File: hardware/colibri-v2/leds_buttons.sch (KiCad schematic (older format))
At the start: 36 parts, among them SW1 SW_PUSH, SW2 SW_PUSH, SW3 SW_PUSH, SW4 SW_PUSH, SW5 SW_PUSH, SW6 SW_PUSH, SW7 SW_PUSH

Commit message: Changes to BOOT0
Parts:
- removed C32: 100nF, symbol C
- added R?: 10K, symbol R
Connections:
- net BOOT0: now also R?.2
- net GND: now also R?.1; no longer SW5.2
- net VDD: now also SW5.2
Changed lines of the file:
@@
 	1    0    0    -1
 $EndComp
-Wire Wire Line
-	1600 3850 1600 3650
-Wire Wire Line
-	2050 2950 2500 2950
-Connection ~ 2350 2950
-Wire Wire Line
-	1350 2950 1750 2950
 $Comp
 L SW_PUSH SW3
@@
 	-1   0    0    1
 $EndComp
-Wire Wire Line
-	3100 4750 3250 4750
-Wire Wire Line
-	3250 4400 3250 4900
 $Comp
 L C C30
@@
 	1    0    0    -1
 $EndComp
-Wire Wire Line
-	3250 5650 3250 5600
-Connection ~ 3250 4750
-Wire Wire Line
-	2350 5650 2350 5400
-Wire Wire Line
-	2050 4750 2500 4750
-Wire Wire Line
-	2350 5100 2350 4750
-Connection ~ 2350 4750
-Wire Wire Line
-	1750 4750 1350 4750
 $Comp
 L R R27
@@
 	-1   0    0    1
 $EndComp
-Wire Wire Line
-	3250 5300 3250 5200
 $Comp
 L SW_PUSH SW4
@@
 	-1   0    0    1
 $EndComp
-Wire Wire Line
-	3100 6600 3250 6600
-Wire Wire Line
-	3250 6250 3250 6750
 $Comp
 L C C31
@@
 	1    0    0    -1
 $EndComp
-Wire Wire Line
-	3250 7500 3250 7450
-Connection ~ 3250 6600
-Wire Wire Line
-	2350 7500 2350 7250
-Wire Wire Line
-	2050 6600 2500 6600
-Wire Wire Line
-	2350 6950 2350 6600
-Connection ~ 2350 6600
-Wire Wire Line
-	1750 6600 1350 6600
 $Comp
 L R R28
@@
 	-1   0    0    1
 $EndComp
-Wire Wire Line
-	3250 7150 3250 7050
 $Comp
 L SW_PUSH SW6
@@
 	-1   0    0    1
 $EndComp
-Wire Wire Line
-	6050 2950 6200 2950
-Wire Wire Line
-	6200 2600 6200 3100
 $Comp
 L C C33
@@
 	1    0    0    -1
 $EndComp
-Wire Wire Line
-	6200 3850 6200 3800
-Connection ~ 6200 2950
-Wire Wire Line
-	5300 3850 5300 3600
-Wire Wire Line
-	5000 2950 5450 2950
-Wire Wire Line
-	5300 3300 5300 2950
-Connection ~ 5300 2950
-Wire Wire Line
-	4700 2950 4300 2950
 $Comp
 L R R33
@@
 	-1   0    0    1
 $EndComp
-Wire Wire Line
-	6200 3500 6200 3400
 $Comp
 L SW_PUSH SW7
@@
 	-1   0    0    1
 $EndComp
-Wire Wire Line
-	6050 4750 6200 4750
-Wire Wire Line
-	6200 4400 6200 4900
 $Comp
 L C C34
@@
 	1    0    0    -1
 $EndComp
-Wire Wire Line
-	6200 5650 6200 5600
-Connection ~ 6200 4750
-Wire Wire Line
-	5300 5650 5300 5400
-Wire Wire Line
-	5000 4750 5450 4750
-Wire Wire Line
-	5300 5100 5300 4750
-Connection ~ 5300 4750
-Wire Wire Line
-	4700 4750 4300 4750
 $Comp
 L R R34
@@
 	-1   0    0    1
 $EndComp
-Wire Wire Line
-	6200 5300 6200 5200
 $Comp
 L VDD #PWR24
@@
 	1    0    0    -1
 $EndComp
-Wire Wire Line
-	3250 1750 3250 1200
-Wire Wire Line
-	3250 1200 3100 1200
 Text HLabel 1350 1200 0    60   Output ~ 0
 RESET#
@@
 	0    1    1    0
 $EndComp
-Wire Wire Line
-	10100 1200 9650 1200
-Wire Wire Line
-	9650 1500 10100 1500
-Connection ~ 10100 1500
-Wire Wire Line
-	9650 1800 10100 1800
-Connection ~ 10100 1800
-Wire Wire Line
-	10100 2100 9650 2100
-Wire Wire Line
-	8900 1200 9250 1200
-Wire Wire Line
-	8900 1500 9250 1500
-Wire Wire Line
-	8900 1800 9250 1800
-Wire Wire Line
-	8900 2100 9250 2100
 Text HLabel 8200 1200 0    60   Input ~ 0
 LED1
@@
 Text HLabel 8200 2100 0    60   Input ~ 0
 LED4
-Wire Wire Line
-	8200 1200 8600 1200
-Wire Wire Line
-	8200 1500 8600 1500
-Wire Wire Line
-	8200 1800 8600 1800
-Wire Wire Line
-	8200 2100 8600 2100
 $Comp
 L GND #PWR23
@@
 	1    0    0    -1
 $EndComp
-$Comp
-L C C32
-U 1 1 56075502
-P 5300 1450
-F 0 "C32" H 5325 1550 50  0000 L CNN
-F 1 "100nF" H 5325 1350 50  0000 L CNN
-F 2 "" H 5338 1300 30  0000 C CNN
-F 3 "" H 5300 1450 60  0000 C CNN
-	1    5300 1450
-	1    0    0    -1
-$EndComp
-$Comp
-L GND #PWR30
-U 1 1 56075508
-P 5300 1750
-F 0 "#PWR30" H 5300 1500 50  0001 C CNN
-F 1 "GND" H 5300 1600 50  0000 C CNN
-F 2 "" H 5300 1750 60  0000 C CNN
-F 3 "" H 5300 1750 60  0000 C CNN
-	1    5300 1750
-	1    0    0    -1
-$EndComp
-Wire Wire Line
-	5300 1600 5300 1750
-Wire Wire Line
-	6200 1750 6200 1200
-Wire Wire Line
-	6200 1200 6050 1200
-Wire Wire Line
-	5300 1200 5300 1300
-Wire Wire Line
-	4300 1200 5450 1200
-Connection ~ 5300 1200
 Text HLabel 4300 1200 0    60   Output ~ 0
 BOOT0
-$Comp
-L GND #PWR33
-U 1 1 56075518
-P 6200 1750
-F 0 "#PWR33" H 6200 1500 50  0001 C CNN
-F 1 "GND" H 6200 1600 50  0000 C CNN
-F 2 "" H 6200 1750 60  0000 C CNN
-F 3 "" H 6200 1750 60  0000 C CNN
-	1    6200 1750
-	1    0    0    -1
-$EndComp
 $Comp
 L R R?
@@
 	0    1    1    0
 $EndComp
-Wire Wire Line
-	1350 1200 1750 1200
-Wire Wire Line
-	2050 1200 2500 1200
-Wire Wire Line
-	2350 2400 2350 2500
-Wire Wire Line
-	2350 2800 2350 2950
-Wire Wire Line
-	1600 3350 1600 2950
-Connection ~ 1600 2950
 $Comp
 L GND #PWR?
@@
 	1    0    0    -1
 $EndComp
-Wire Wire Line
-	3100 2950 3300 2950
-Wire Wire Line
-	3300 2950 3300 3850
-Wire Wire Line
-	10100 950  10100 2100
 $Comp
 L VDD #PWR?
@@
 	1    0    0    -1
 $EndComp
+$Comp
+L R R?
+U 1 1 5622C644
+P 4900 1550
+F 0 "R?" V 4980 1550 50  0000 C CNN
+F 1 "10K" V 4900 1550 50  0000 C CNN
+F 2 "" V 4830 1550 30  0000 C CNN
+F 3 "" H 4900 1550 30  0000 C CNN
+	1    4900 1550
+	-1   0    0    1
+$EndComp
+$Comp
+L VDD #PWR?
+U 1 1 5622CB72
+P 6200 1000
+F 0 "#PWR?" H 6200 850 50  0001 C CNN
+F 1 "VDD" H 6200 1150 50  0000 C CNN
+F 2 "" H 6200 1000 60  0000 C CNN
+F 3 "" H 6200 1000 60  0000 C CNN
+	1    6200 1000
+	1    0    0    -1
+$EndComp
+$Comp
+L GND #PWR?
+U 1 1 5622D3C9
+P 4900 1900
+F 0 "#PWR?" H 4900 1650 50  0001 C CNN
+F 1 "GND" H 4900 1750 50  0000 C CNN
+F 2 "" H 4900 1900 60  0000 C CNN
+F 3 "" H 4900 1900 60  0000 C CNN
+	1    4900 1900
+	1    0    0    -1
+$EndComp
+Wire Wire Line
+	1600 3850 1600 3650
+Wire Wire Line
+	2050 2950 2500 2950
+Connection ~ 2350 2950
+Wire Wire Line
+	1350 2950 1750 2950
+Wire Wire Line
+	3100 4750 3250 4750
+Wire Wire Line
+	3250 4400 3250 4900
+Wire Wire Line
+	3250 5650 3250 5600
+Connection ~ 3250 4750
+Wire Wire Line
+	2350 5650 2350 5400
+Wire Wire Line
+	2050 4750 2500 4750
+Wire Wire Line
+	2350 5100 2350 4750
+Connection ~ 2350 4750
+Wire Wire Line
+	1750 4750 1350 4750
+Wire Wire Line
+	3250 5300 3250 5200
+Wire Wire Line
+	3100 6600 3250 6600
+Wire Wire Line
+	3250 6250 3250 6750
+Wire Wire Line
+	3250 7500 3250 7450
+Connection ~ 3250 6600
+Wire Wire Line
+	2350 7500 2350 7250
+Wire Wire Line
+	2050 6600 2500 6600
+Wire Wire Line
+	2350 6950 2350 6600
+Connection ~ 2350 6600
+Wire Wire Line
+	1750 6600 1350 6600
+Wire Wire Line
+	3250 7150 3250 7050
+Wire Wire Line
+	6050 2950 6200 2950
+Wire Wire Line
+	6200 2600 6200 3100
+Wire Wire Line
+	6200 3850 6200 3800
+Connection ~ 6200 2950
+Wire Wire Line
+	5300 3850 5300 3600
+Wire Wire Line
+	5000 2950 5450 2950
+Wire Wire Line
+	5300 3300 5300 2950
+Connection ~ 5300 2950
+Wire Wire Line
+	4700 2950 4300 2950
+Wire Wire Line
+	6200 3500 6200 3400
+Wire Wire Line
+	6050 4750 6200 4750
+Wire Wire Line
+	6200 4400 6200 4900
+Wire Wire Line
+	6200 5650 6200 5600
+Connection ~ 6200 4750
+Wire Wire Line
+	5300 5650 5300 5400
+Wire Wire Line
+	5000 4750 5450 4750
+Wire Wire Line
+	5300 5100 5300 4750
+Connection ~ 5300 4750
+Wire Wire Line
+	4700 4750 4300 4750
+Wire Wire Line
+	6200 5300 6200 5200
+Wire Wire Line
+	3250 1750 3250 1200
+Wire Wire Line
+	3250 1200 3100 1200
+Wire Wire Line
+	10100 1200 9650 1200
+Wire Wire Line
+	9650 1500 10100 1500
+Connection ~ 10100 1500
+Wire Wire Line
+	9650 1800 10100 1800
+Connection ~ 10100 1800
+Wire Wire Line
+	10100 2100 9650 2100
+Wire Wire Line
+	8900 1200 9250 1200
+Wire Wire Line
+	8900 1500 9250 1500
+Wire Wire Line
+	8900 1800 9250 1800
+Wire Wire Line
+	8900 2100 9250 2100
+Wire Wire Line
+	8200 1200 8600 1200
+Wire Wire Line
+	8200 1500 8600 1500
+Wire Wire Line
+	8200 1800 8600 1800
+Wire Wire Line
+	8200 2100 8600 2100
+Wire Wire Line
+	1350 1200 1750 1200
+Wire Wire Line
+	2050 1200 2500 1200
+Wire Wire Line
+	2350 2400 2350 2500
+Wire Wire Line
+	2350 2800 2350 2950
+Wire Wire Line
+	1600 3350 1600 2950
+Connection ~ 1600 2950
+Wire Wire Line
+	3100 2950 3300 2950
+Wire Wire Line
+	3300 2950 3300 3850
+Wire Wire Line
+	10100 950  10100 2100
 Connection ~ 10100 1200
+Wire Wire Line
+	6050 1200 6200 1200
+Wire Wire Line
+	6200 1200 6200 1000
+Wire Wire Line
+	4300 1200 5450 1200
+Wire Wire Line
+	4900 1400 4900 1200
+Connection ~ 4900 1200
+Wire Wire Line
+	4900 1900 4900 1700
 $EndSCHEMATC

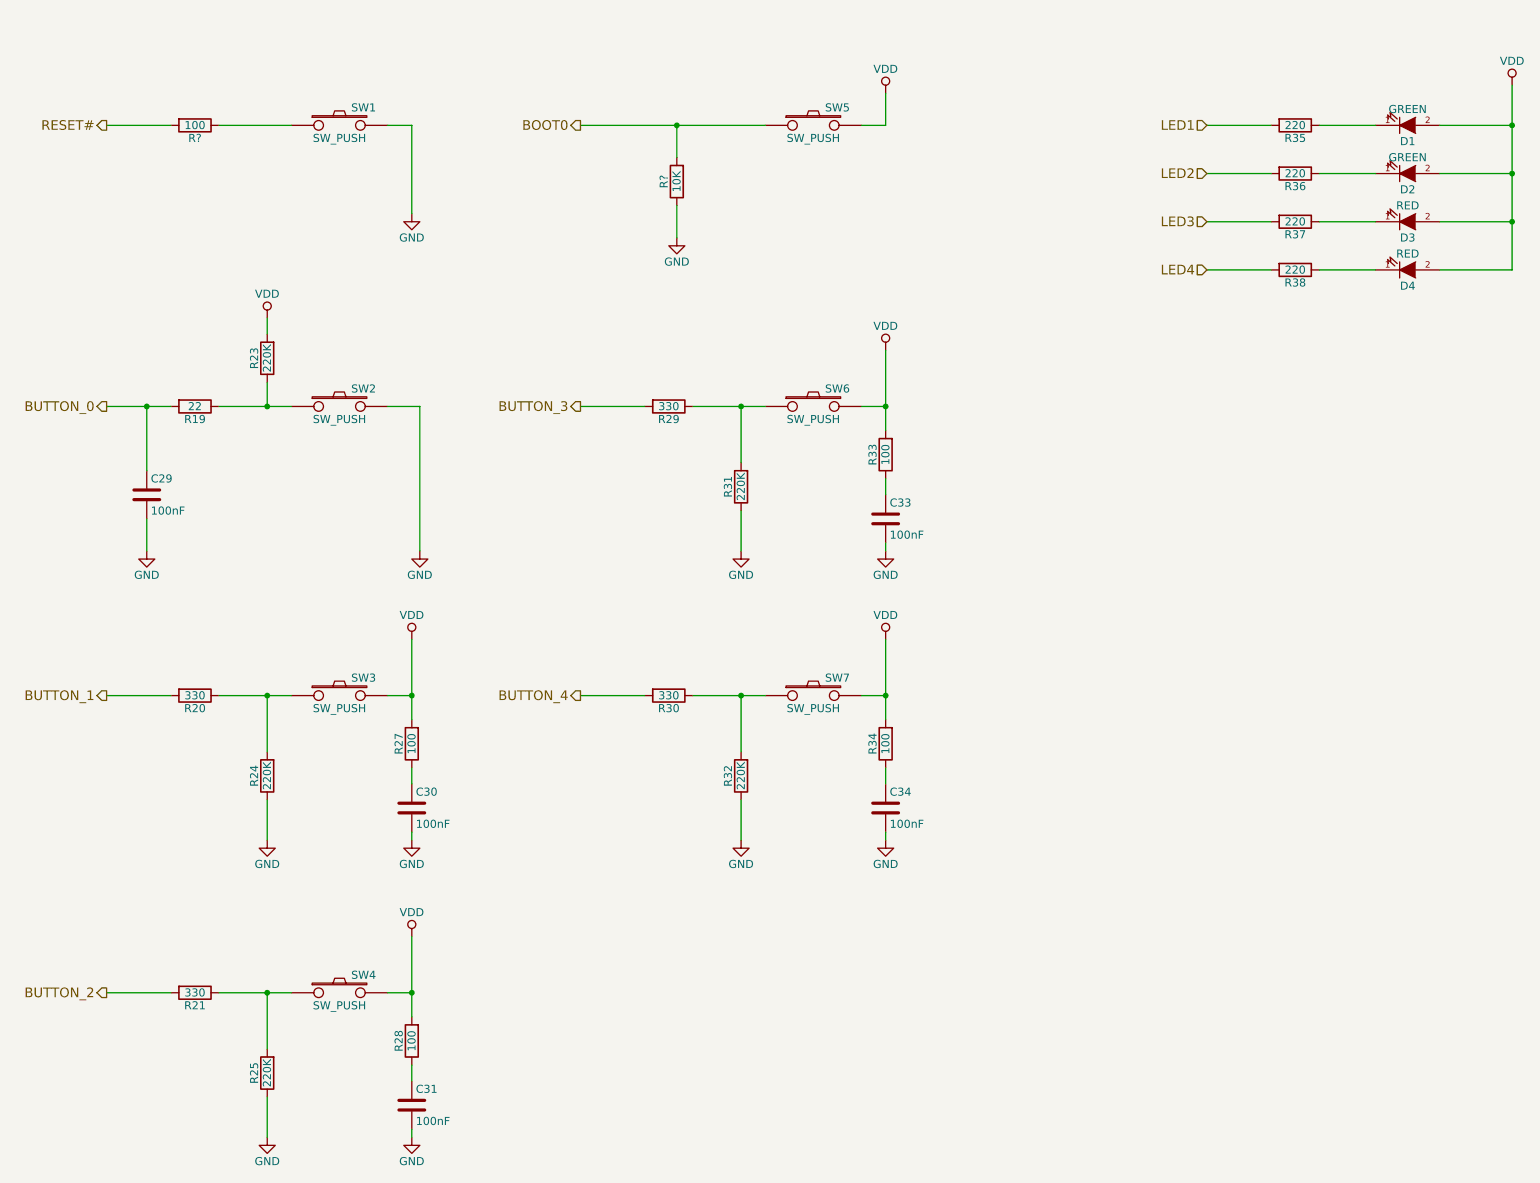
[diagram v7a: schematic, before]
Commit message: Reworked the buttons/leds sheet
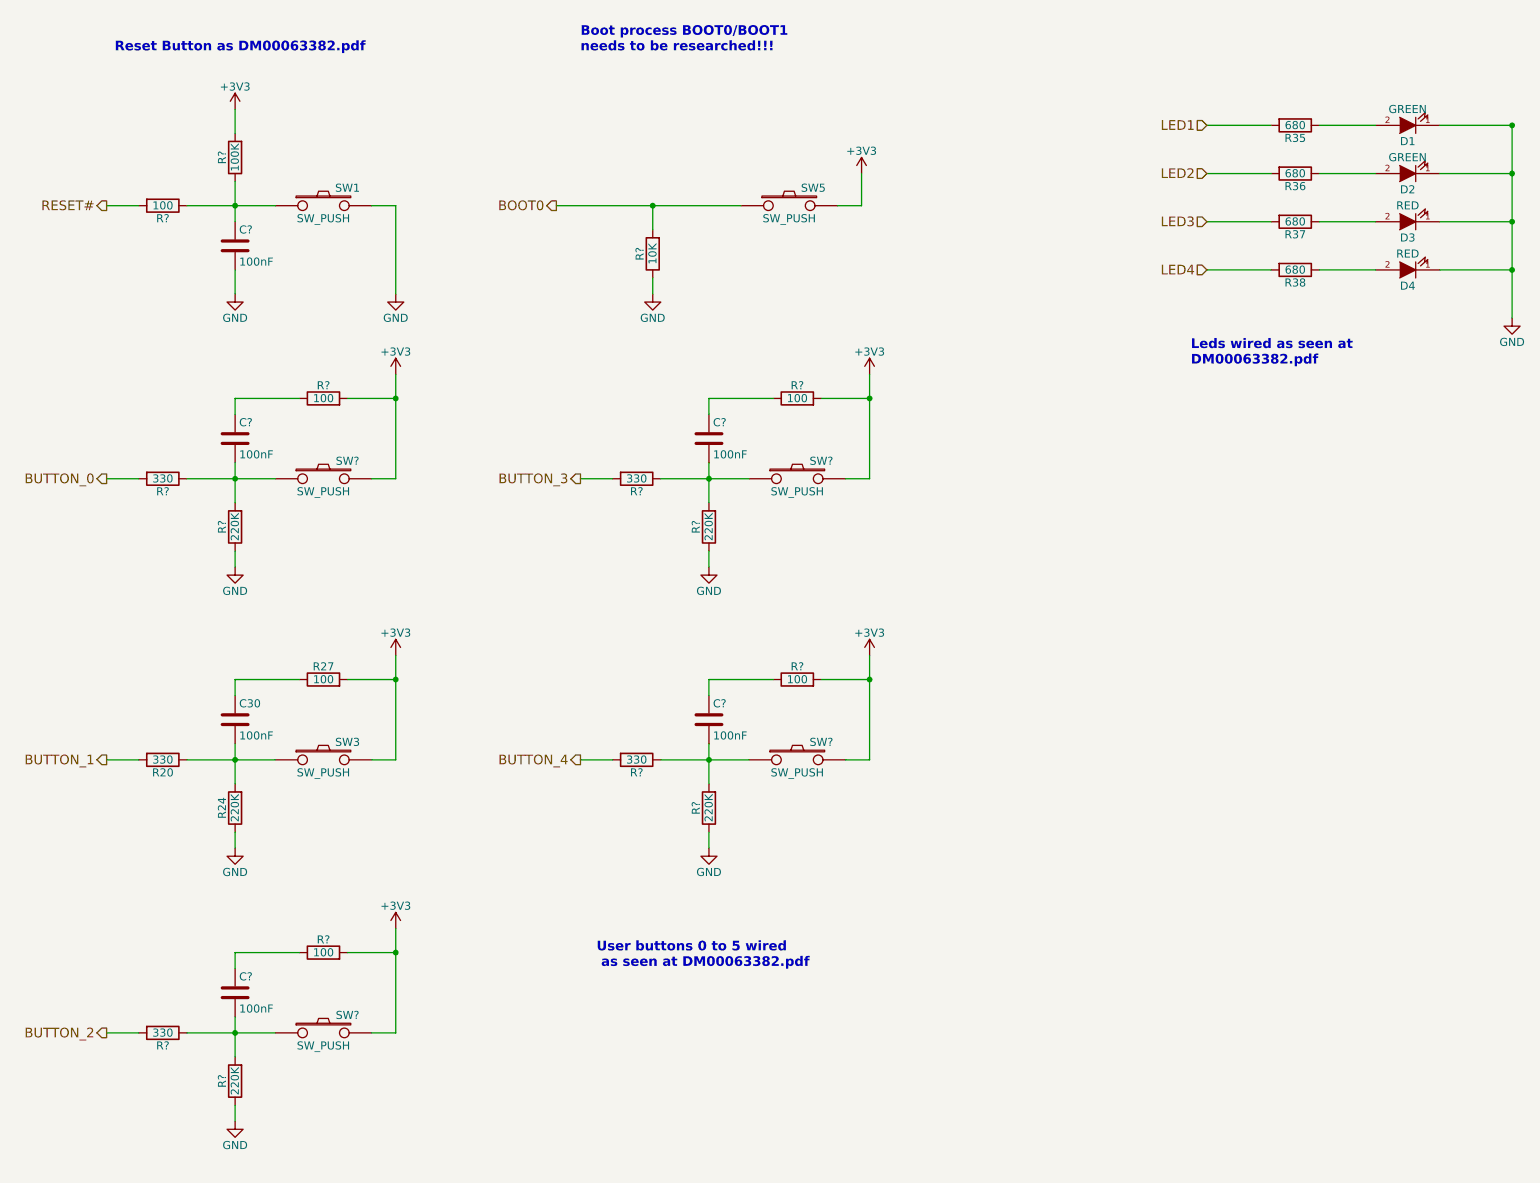
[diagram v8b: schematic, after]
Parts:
- removed C29, C31, C33, C34: 100nF, symbol C
- removed R19: 22, symbol R
- removed R21, R29, R30: 330, symbol R
- removed R23, R25, R31, R32: 220K, symbol R
- removed R28, R33, R34: 100, symbol R
- removed SW2, SW4, SW6, SW7: SW_PUSH, symbol SW_PUSH
- added C? (x5): 100nF, symbol C
- added R? (x4): 330, symbol R
- added R? (x4): 220K, symbol R
- added R? (x4): 100, symbol R
- added R?: 100K, symbol R
- added SW? (x4): SW_PUSH, symbol SW_PUSH
- R35, R36, R37, R38: value 220 -> 680
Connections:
- net BUTTON_0: now also R?.2
- net BUTTON_2: now also R?.2
- net BUTTON_3: now also R?.2
- net BUTTON_4: now also R?.2
- net GND: now also D1.1 (K), D2.1 (K), D3.1 (K), D4.1 (K), C?.2, R?.1, R?.1, R?.1, R?.1; no longer C30.2
- net at R20.1, R24.2, SW3.1: now also C30.2
- net at R?.1, SW1.1: now also C?.1, R?.1
- net at R35.1: now also D1.2 (A); no longer D1.1 (K)
- net at R36.1: now also D2.2 (A); no longer D2.1 (K)
- net at R37.1: now also D3.2 (A); no longer D3.1 (K)
- net at R38.1: now also D4.2 (A); no longer D4.1 (K)
- removed net VDD: D1.2 (A), D2.2 (A), D3.2 (A), D4.2 (A), R27.2, SW3.2, SW5.2
- new net: C?.2, R?.1, R?.2, SW?.1 (x4)
- new net: C?.1, R?.1 (x4)
- new net +3V3: R27.2, R?.2, R?.2, R?.2, R?.2, R?.2, SW3.2, SW5.2, SW?.2, SW?.2, SW?.2, SW?.2
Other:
- note added: "Boot process BOOT0/BOOT1\nneeds to be researched!!!"
- note added: "Leds wired as seen at\nDM00063382.pdf"
- note added: "Reset Button as DM00063382.pdf"
- note added: "User buttons 0 to 5 wired\n as seen at DM00063382.pdf"
- moved on the sheet: C30, R20, R24, R27, R?, SW1, SW3, SW5
